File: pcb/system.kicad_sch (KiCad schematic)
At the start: 24 parts, among them J1 USB_C_Receptacle_USB2.0_16P, J6 Conn_01x04, U1 RP2040, U2 W25Q128JVS, U5 MB85RS1MT

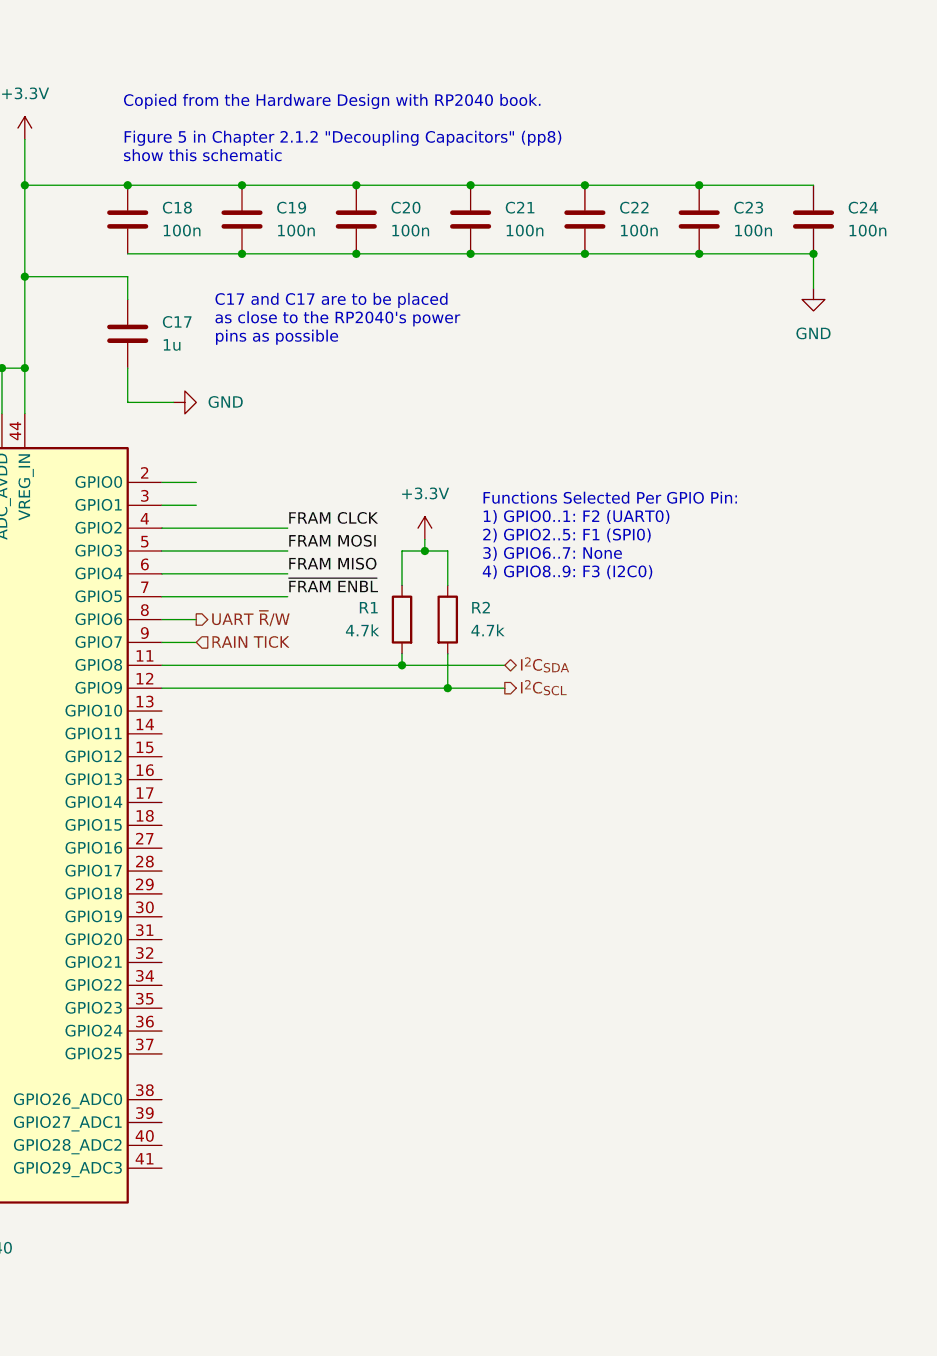
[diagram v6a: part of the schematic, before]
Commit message: feat: reserved connections for SX1278 lora module
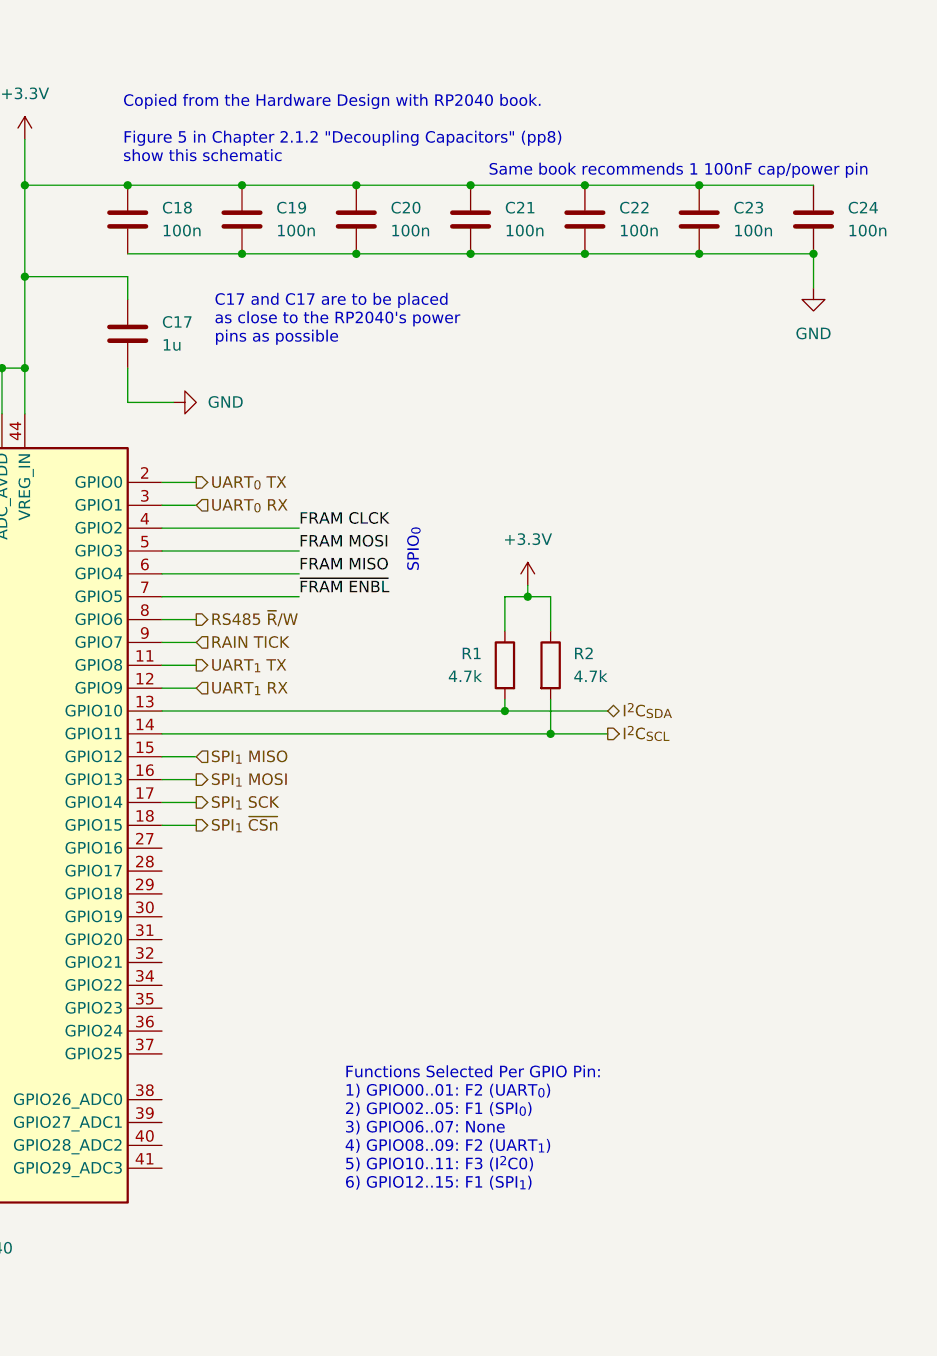
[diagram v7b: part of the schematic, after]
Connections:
- net I^{2}C_{SCL}: now also U1.14 (GPIO11); no longer U1.12 (GPIO9)
- net I^{2}C_{SDA}: now also U1.13 (GPIO10); no longer U1.11 (GPIO8)
- net SPI_{1} MISO: now reaches U1.15 (GPIO12)
- net SPI_{1} MOSI: now reaches U1.16 (GPIO13)
- net SPI_{1} SCK: now reaches U1.17 (GPIO14)
- net SPI_{1} ~{CSn}: now reaches U1.18 (GPIO15)
- net UART_{0} TX: now reaches U1.2 (GPIO0)
- net UART_{0} RX: now reaches U1.3 (GPIO1)
- net UART ~{R}/W renamed RS485 ~{R}/W
- new net UART_{1} RX: U1.12 (GPIO9)
- new net UART_{1} TX: U1.11 (GPIO8)
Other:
- note added: "Functions Selected Per GPIO Pin: 1) GPIO00..01: F2 (UART_{0}) 2) GPIO02..05: F1 (SPI_{0}) 3) GPIO06..07: None 4) GPIO08..09: F2 (UART_{1}) 5) GPIO10..11: F3 (I^{2}C0) 6) GPIO12..15: F1 (SPI_{1})"
- note added: "SPIO_{0}"
- note added: "Same book recommends 1 100nF cap/power pin"
- note removed: "Functions Selected Per GPIO Pin: 1) GPIO0..1: F2 (UART0) 2) GPIO2..5: F1 (SPI0) 3) GPIO6..7: None 4) GPIO8..9: F3 (I2C0)"
- moved on the sheet: R1, R2
